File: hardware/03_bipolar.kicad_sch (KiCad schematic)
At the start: 20 parts, among them U4 TPS65131RGER

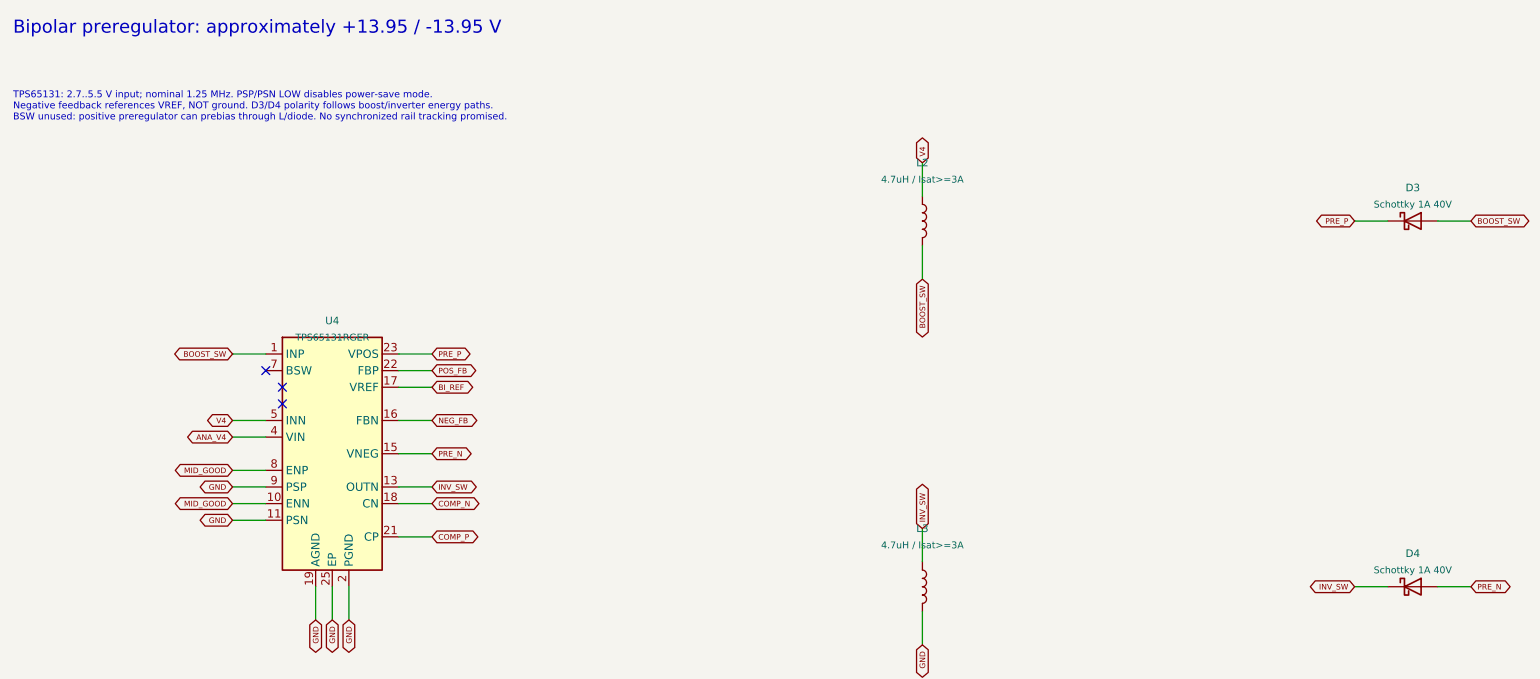
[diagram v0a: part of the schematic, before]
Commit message: Refine USB-C PD input safety review and validate unrouted KiCad prototype
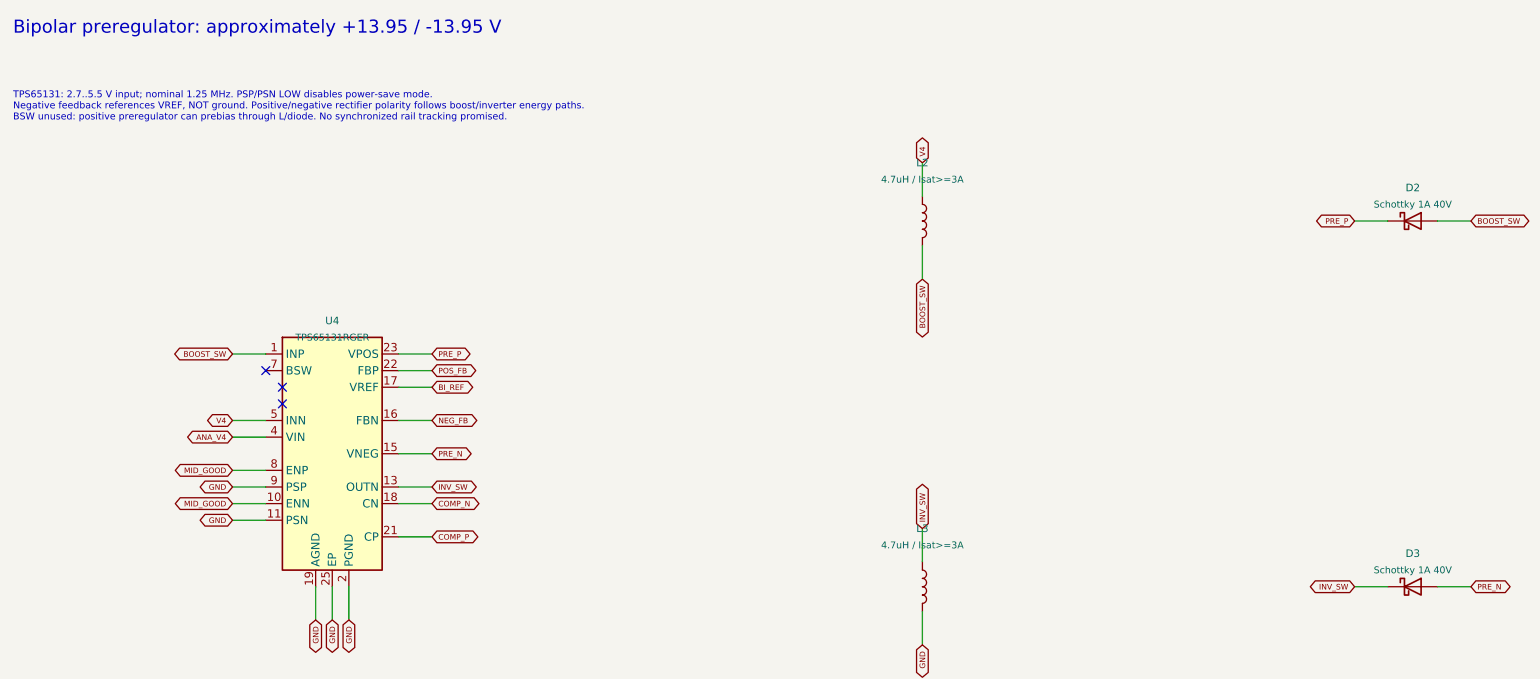
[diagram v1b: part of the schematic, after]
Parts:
- removed D4: Schottky 1A 40V, symbol BigModular:Device_D_Schottky
- added D2: Schottky 1A 40V, symbol BigModular:Device_D_Schottky
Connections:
- net BOOST_SW: now also D2.2 (A); no longer D3.2 (A)
- net INV_SW: now also D3.1 (K)
- net PRE_N: now also D3.2 (A)
- net PRE_P: now also D2.1 (K); no longer D3.1 (K)
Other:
- note added: "TPS65131: 2.7..5.5 V input; nominal 1.25 MHz. PSP/PSN LOW disables power-save mode. Negative feedback references VREF, NOT ground. Positive/negative rectifier polarity follows boost/inverter energy paths. BSW unused: positive preregulator can prebias through L/diode. No synchronized rail tracking promised."
- note removed: "TPS65131: 2.7..5.5 V input; nominal 1.25 MHz. PSP/PSN LOW disables power-save mode. Negative feedback references VREF, NOT ground. D3/D4 polarity follows boost/inverter energy paths. BSW unused: positive preregulator can prebias through L/diode. No synchronized rail tracking promised."
- moved on the sheet: D3
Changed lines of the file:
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@@
 (kicad_sch (version 20250114) (generator "eeschema") (paper "A3") (title_block (title "Bipolar preregulator: approximately +13.95 / -13.95 V") (date "2026-09-24") (rev "A0 ENGINEERING PROTOTYPE") (company "Big Modular") (comment 1 "NOT FOR FABRICATION - UNROUTED PLACEMENT SCAFFOLDS"))
 (text "Bipolar preregulator: approximately +13.95 / -13.95 V" (at 16 15 0) (effects (font (size 2 2)) (justify left)))
-(text "TPS65131: 2.7..5.5 V input; nominal 1.25 MHz. PSP/PSN LOW disables power-save mode.\nNegative feedback references VREF, NOT ground. D3/D4 polarity follows boost/inverter energy paths.\nBSW unused: positive preregulator can prebias through L/diode. No synchronized rail tracking promised." (at 16 27 0) (effects (font (size 1.05 1.05)) (justify left)))
+(text "TPS65131: 2.7..5.5 V input; nominal 1.25 MHz. PSP/PSN LOW disables power-save mode.\nNegative feedback references VREF, NOT ground. Positive/negative rectifier polarity follows boost/inverter energy paths.\nBSW unused: positive preregulator can prebias through L/diode. No synchronized rail tracking promised." (at 16 27 0) (effects (font (size 1.05 1.05)) (justify left)))
 (wire (pts (xy 54.61 64.77000000000001) (xy 49.53 64.77)) (stroke (width 0) (type default)))
 (global_label "BOOST_SW" (shape bidirectional) (at 49.53 64.77 180) (effects (font (size 0.85 0.85))))
@@
 (wire (pts (xy 233.68 44.45) (xy 238.76 44.45)) (stroke (width 0) (type default)))
 (global_label "BOOST_SW" (shape bidirectional) (at 238.76 44.45 0) (effects (font (size 0.85 0.85))))
-(symbol (lib_id "BigModular:Device_D_Schottky") (at 229.87 44.45 0) (unit 1) (in_bom yes) (on_board yes) (dnp no)(property "Reference" "D3" (at 229.87 39.370000000000005 0) (effects (font (size 1.15 1.15))))(property "Value" "Schottky 1A 40V" (at 229.87 41.910000000000004 0) (effects (font (size 1.05 1.05))))(property "Footprint" "" (at 229.87 44.45 0) (effects (font (size 1 1)) hide))(property "MPN" "" (at 229.87 44.45 0) (effects (font (size 1 1)) hide))(property "LCSC" "" (at 229.87 44.45 0) (effects (font (size 1 1)) hide))(property "NOTE" "" (at 229.87 44.45 0) (effects (font (size 1 1)) hide))(pin "1")(pin "2")(instances (project "big_modular" (path "/d567704c-57ad-5df1-b183-cadb01fd8972/6ae7aeb3-31bb-5580-ba62-4d68a0707add" (reference "D3") (unit 1)))) )
+(symbol (lib_id "BigModular:Device_D_Schottky") (at 229.87 44.45 0) (unit 1) (in_bom yes) (on_board yes) (dnp no)(property "Reference" "D2" (at 229.87 39.370000000000005 0) (effects (font (size 1.15 1.15))))(property "Value" "Schottky 1A 40V" (at 229.87 41.910000000000004 0) (effects (font (size 1.05 1.05))))(property "Footprint" "" (at 229.87 44.45 0) (effects (font (size 1 1)) hide))(property "MPN" "" (at 229.87 44.45 0) (effects (font (size 1 1)) hide))(property "LCSC" "" (at 229.87 44.45 0) (effects (font (size 1 1)) hide))(property "NOTE" "" (at 229.87 44.45 0) (effects (font (size 1 1)) hide))(pin "1")(pin "2")(instances (project "big_modular" (path "/d567704c-57ad-5df1-b183-cadb01fd8972/6ae7aeb3-31bb-5580-ba62-4d68a0707add" (reference "D2") (unit 1)))) )
 (wire (pts (xy 154.94 96.52) (xy 154.94 91.44)) (stroke (width 0) (type default)))
 (global_label "INV_SW" (shape bidirectional) (at 154.94 91.44 90) (effects (font (size 0.85 0.85))))
@@
 (wire (pts (xy 233.68 100.33) (xy 238.76 100.33)) (stroke (width 0) (type default)))
 (global_label "PRE_N" (shape bidirectional) (at 238.76 100.33 0) (effects (font (size 0.85 0.85))))
-(symbol (lib_id "BigModular:Device_D_Schottky") (at 229.87 100.33 0) (unit 1) (in_bom yes) (on_board yes) (dnp no)(property "Reference" "D4" (at 229.87 95.25 0) (effects (font (size 1.15 1.15))))(property "Value" "Schottky 1A 40V" (at 229.87 97.79 0) (effects (font (size 1.05 1.05))))(property "Footprint" "" (at 229.87 100.33 0) (effects (font (size 1 1)) hide))(property "MPN" "" (at 229.87 100.33 0) (effects (font (size 1 1)) hide))(property "LCSC" "" (at 229.87 100.33 0) (effects (font (size 1 1)) hide))(property "NOTE" "" (at 229.87 100.33 0) (effects (font (size 1 1)) hide))(pin "1")(pin "2")(instances (project "big_modular" (path "/d567704c-57ad-5df1-b183-cadb01fd8972/6ae7aeb3-31bb-5580-ba62-4d68a0707add" (reference "D4") (unit 1)))) )
+(symbol (lib_id "BigModular:Device_D_Schottky") (at 229.87 100.33 0) (unit 1) (in_bom yes) (on_board yes) (dnp no)(property "Reference" "D3" (at 229.87 95.25 0) (effects (font (size 1.15 1.15))))(property "Value" "Schottky 1A 40V" (at 229.87 97.79 0) (effects (font (size 1.05 1.05))))(property "Footprint" "" (at 229.87 100.33 0) (effects (font (size 1 1)) hide))(property "MPN" "" (at 229.87 100.33 0) (effects (font (size 1 1)) hide))(property "LCSC" "" (at 229.87 100.33 0) (effects (font (size 1 1)) hide))(property "NOTE" "" (at 229.87 100.33 0) (effects (font (size 1 1)) hide))(pin "1")(pin "2")(instances (project "big_modular" (path "/d567704c-57ad-5df1-b183-cadb01fd8972/6ae7aeb3-31bb-5580-ba62-4d68a0707add" (reference "D3") (unit 1)))) )
 (wire (pts (xy 304.8 40.64) (xy 304.8 35.56)) (stroke (width 0) (type default)))
 (global_label "PRE_P" (shape bidirectional) (at 304.8 35.56 90) (effects (font (size 0.85 0.85))))
